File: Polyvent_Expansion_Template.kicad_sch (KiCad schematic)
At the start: 1 part, among them J1 09231486921

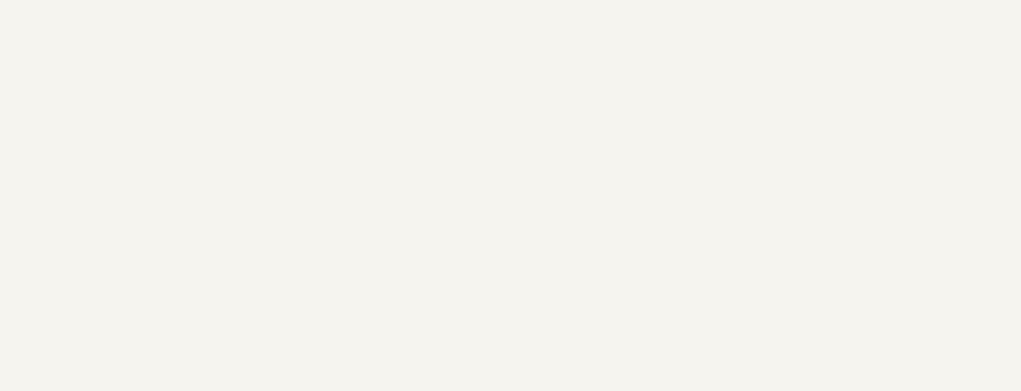
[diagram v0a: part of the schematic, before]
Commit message: Add defaults to schematic and PCB including license and Public Invetion Name. Lock the connector on PCB.
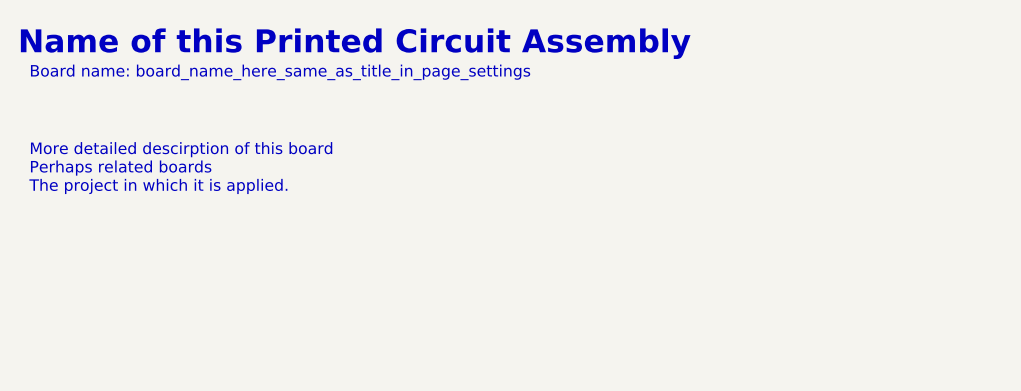
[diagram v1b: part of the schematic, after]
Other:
- note added: "Board name: board_name_here_same_as_title_in_page_settings"
- note added: "More detailed descirption of this board Perhaps related boards The project in which it is applied."
- note added: "Name of this Printed Circuit Assembly"
- company: (none) -> Public Invention
- title: (none) -> board_name_here_same_as_title_in_page_settings
